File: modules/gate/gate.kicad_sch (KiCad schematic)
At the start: 24 parts, among them SW1 MODE SELECT, U1 MCP6002-xSN, U2 ATtiny1616-M, U3 MCP6002-xSN

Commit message: Apply new code changes to the schematic
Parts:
- removed C2: 100nf, Capacitor_SMD:C_0402_1005Metric, symbol Device:C
- removed RV1: 50k, BreadModular_Pots:Potentiometer_RV09, symbol Device:R_Potentiometer
- D1: value LED -> GATE MODE LED
- R3: value 1k -> 100k
- SW1: value MODE SELECT -> GATE MODE SELECT
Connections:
- net CV1: now also INPUT1.3 (Pin_3); no longer INPUT1.2 (Pin_2)
- net CV2: now also INPUT1.4 (Pin_4); no longer INPUT1.3 (Pin_3)
- net ENV_OUT: now also OUTPUT1.4 (Pin_4), OUTPUT1.5 (Pin_5); no longer OUTPUT1.1 (Pin_1)
- net GATE: now also INPUT1.2 (Pin_2), R3.2, U1.5 (+); no longer INPUT1.1 (Pin_1), U2.12 (PB2)
- net GND: now also R3.1
- net MIDI: now also INPUT1.1 (Pin_1), OUTPUT1.1 (Pin_1); no longer INPUT1.4 (Pin_4)
- net at U2.8 (PA7): no longer U1.5 (+)
- net BUFF_GATE: now reaches U1.6 (-), U1.7
- net BUFF_GATE: now also U2.12 (PB2); no longer R3.1
- net at U1.3 (+): now also U2.7 (PA6)
- removed net GATE_OUT: OUTPUT1.4 (Pin_4), OUTPUT1.5 (Pin_5), R3.2
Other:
- moved on the sheet: R7, R8, RV2, RV3, U1B, U3A, U3B

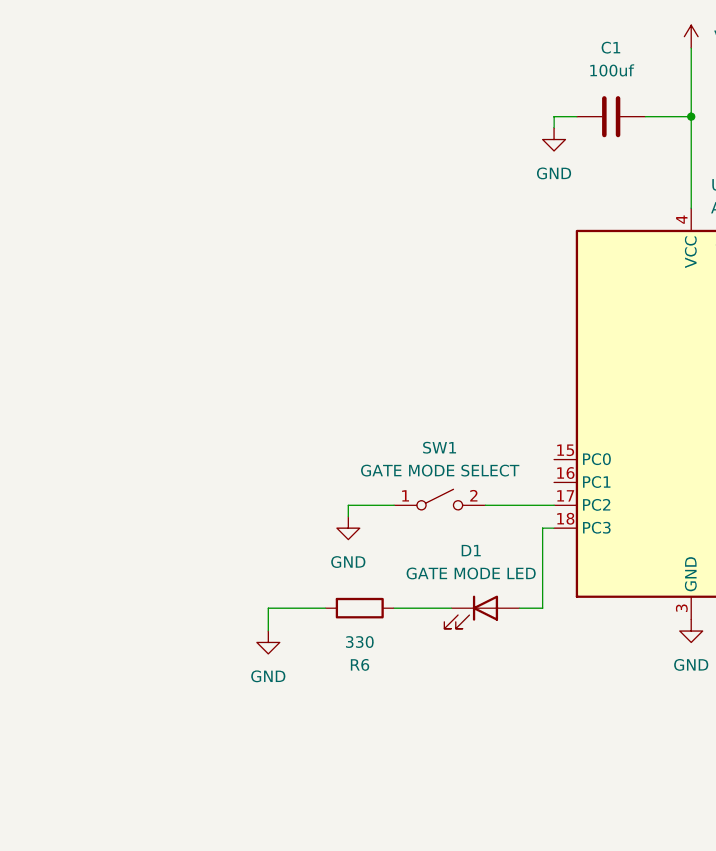
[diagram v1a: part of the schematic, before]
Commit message: Add algo mode select to pcb
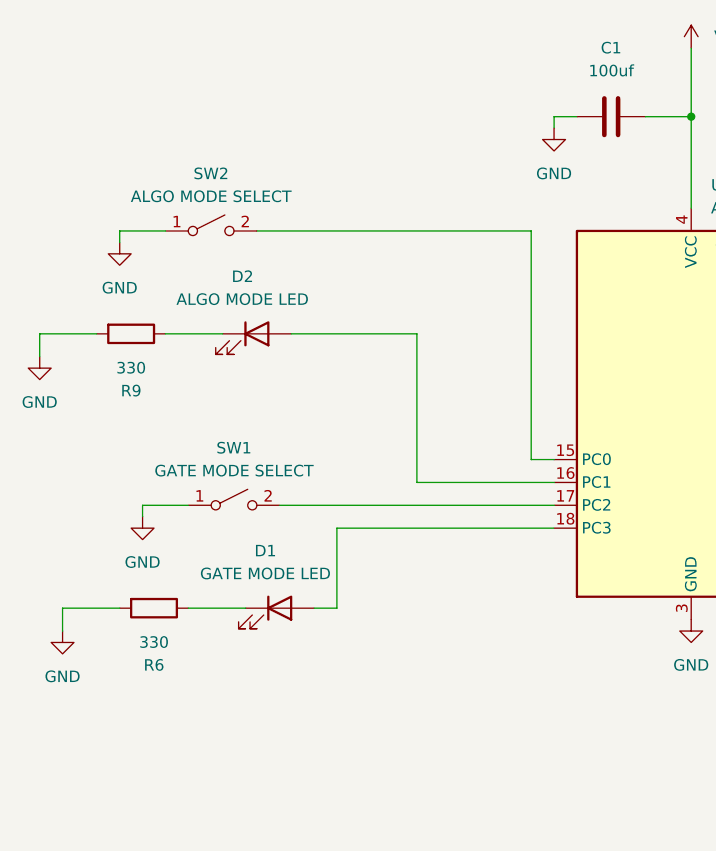
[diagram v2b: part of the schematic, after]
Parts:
- added D2: ALGO MODE LED, LED_SMD:LED_0603_1608Metric, symbol Device:LED
- added R9: 330, Resistor_SMD:R_0402_1005Metric, symbol Device:R
- added SW2: ALGO MODE SELECT, BreadModular_MISC:SPST_TS-1187A-B-A-B, symbol Switch:SW_SPST
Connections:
- net GND: now also R9.2, SW2.1 (A)
- net at U2.15 (PC0): now also SW2.2 (B)
- net at U2.16 (PC1): now also D2.2 (A)
- new net: D2.1 (K), R9.1
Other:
- moved on the sheet: D1, R6, SW1

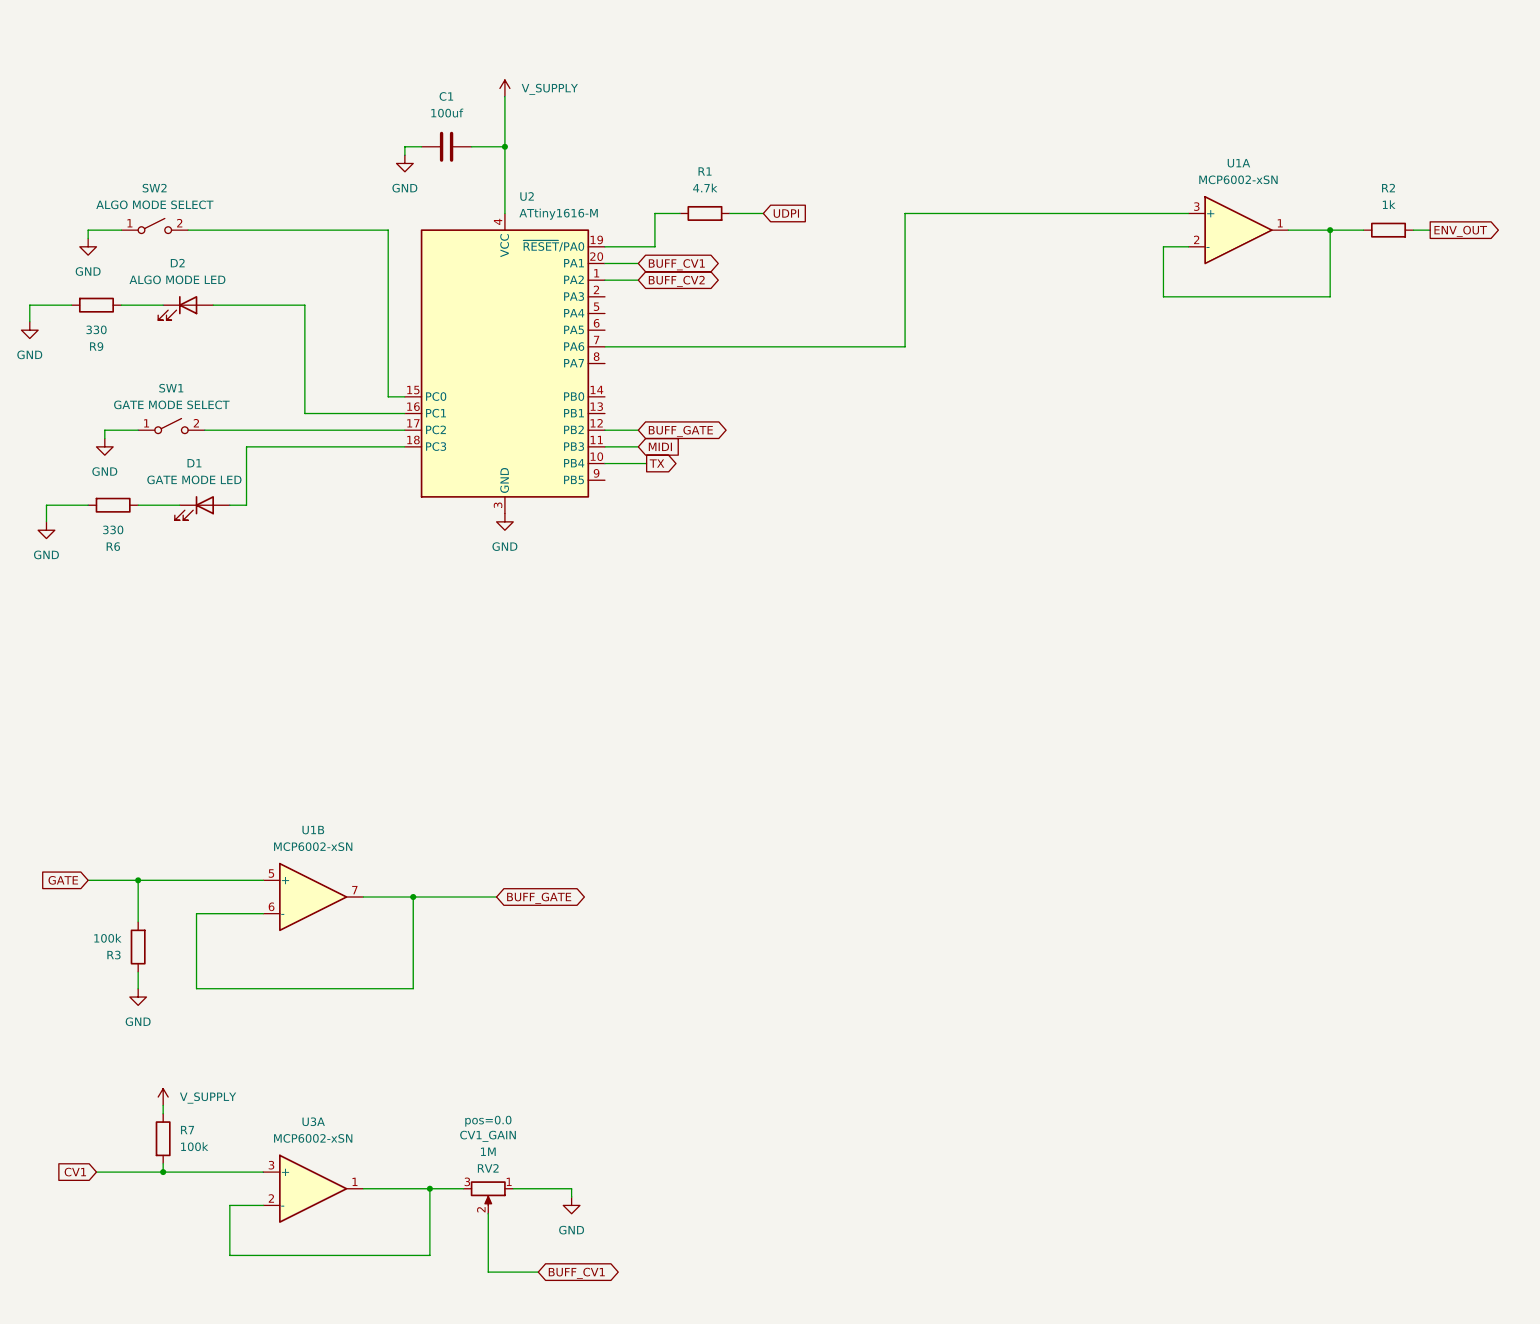
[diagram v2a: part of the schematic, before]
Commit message: Add LED Preview
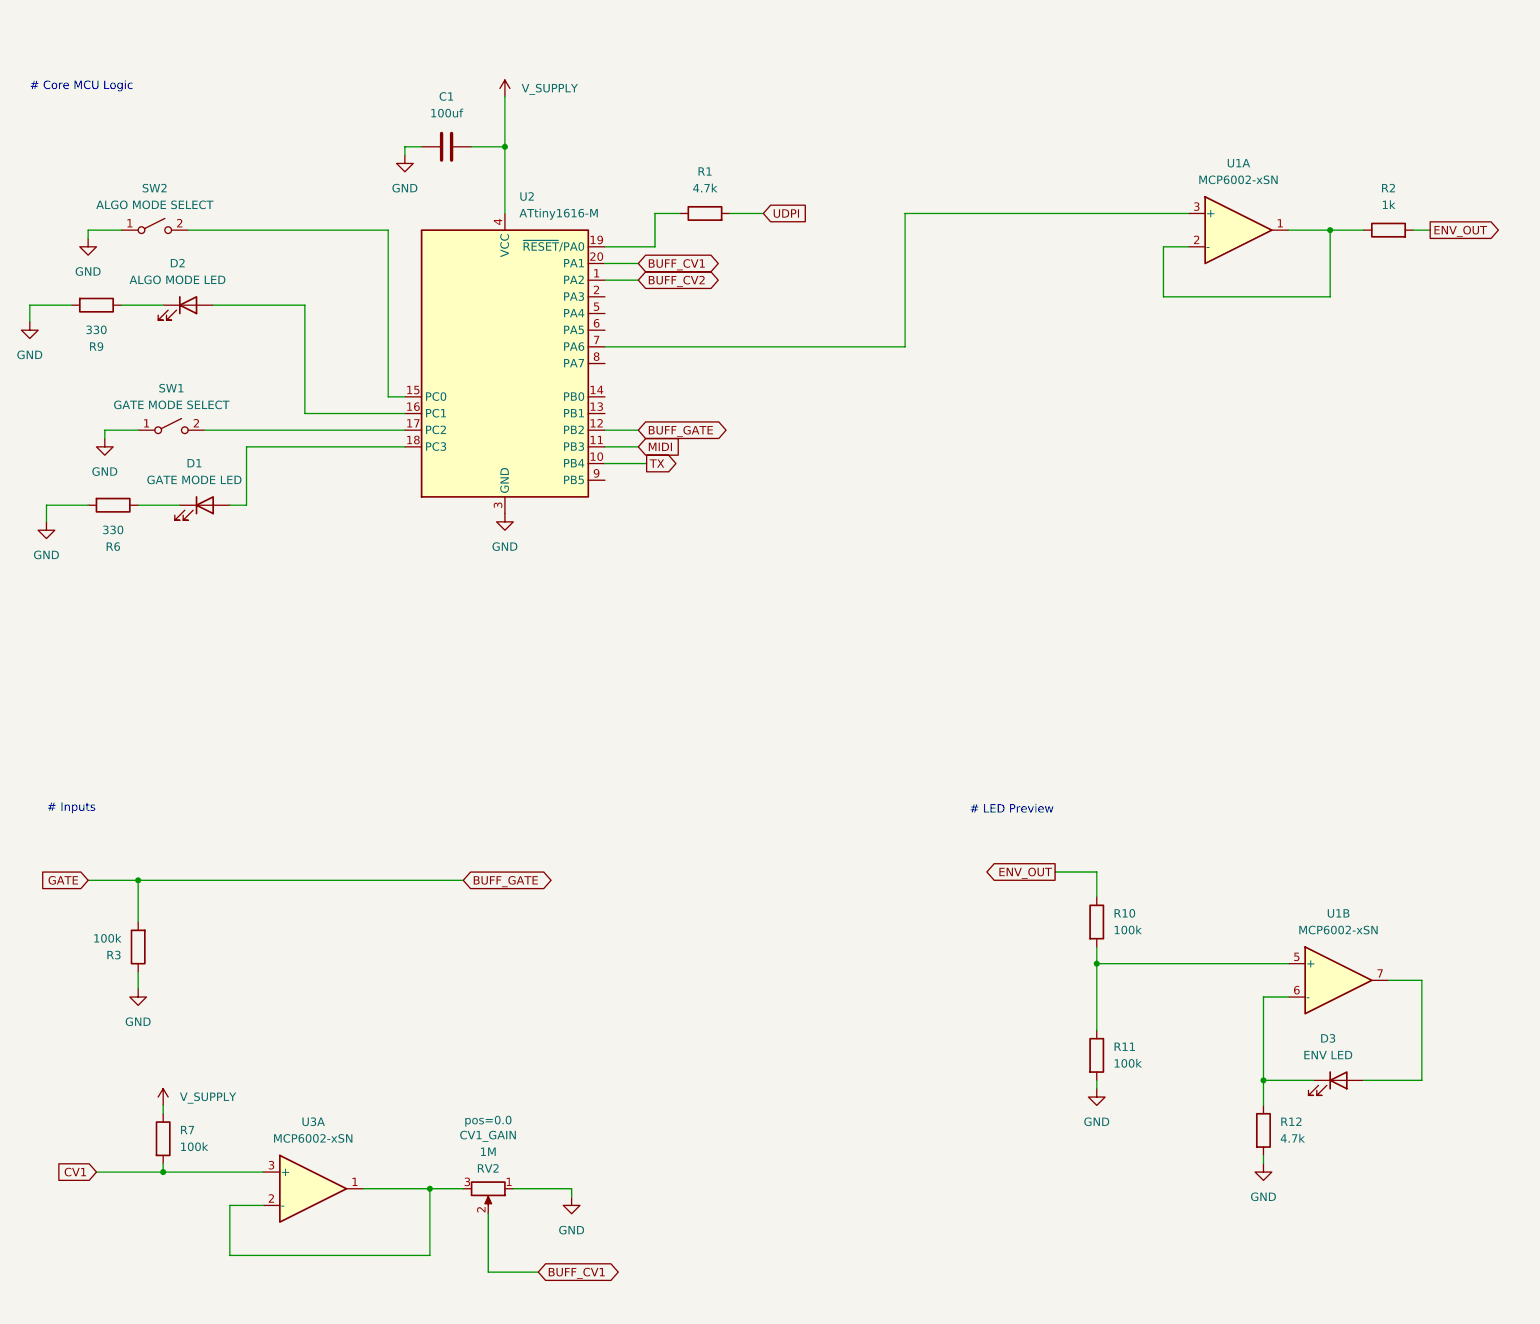
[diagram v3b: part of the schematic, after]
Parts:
- added D3: ENV LED, LED_SMD:LED_0603_1608Metric, symbol Device:LED
- added R10, R11: 100k, Resistor_SMD:R_0402_1005Metric, symbol Device:R
- added R12: 4.7k, Resistor_SMD:R_0402_1005Metric, symbol Device:R
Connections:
- net BUFF_GATE: now also INPUT1.2 (Pin_2), R3.2; no longer U1.6 (-), U1.7
- net ENV_OUT: now also R10.1
- net GND: now also R11.2, R12.2
- removed net GATE: INPUT1.2 (Pin_2), R3.2, U1.5 (+)
- new net: R10.2, R11.1, U1.5 (+)
- new net: D3.1 (K), R12.1, U1.6 (-)
- new net: D3.2 (A), U1.7
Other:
- note added: "# Core MCU Logic"
- note added: "# Inputs"
- note added: "# LED Preview"
- moved on the sheet: U1B
